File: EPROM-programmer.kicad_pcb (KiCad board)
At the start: 2 copper layers, 139.7 x 139.7 mm, 100 parts, among them J1 ZIF-socket, J10 VCC, J2 ISP, J5 GND, J6 Barrel_Jack_Switch, J7 ZIF_VCC, J8 VPP, J9 GND, P1 USB-C, Q1 BC327, Q2 BC327, Q3 BC327, Q4 BC327, Q5 BC327, Q6 BC327, SW1 Reset, U1 ATmega1284-P, U2 MCP2221AxP, U3 MCP4812, U4 LM358, U5 ULN2003, U6 LM317_TO-220, U7 LM317_TO-220, U8 LM7805_TO220, U9 MC34063AP, Y1 20M

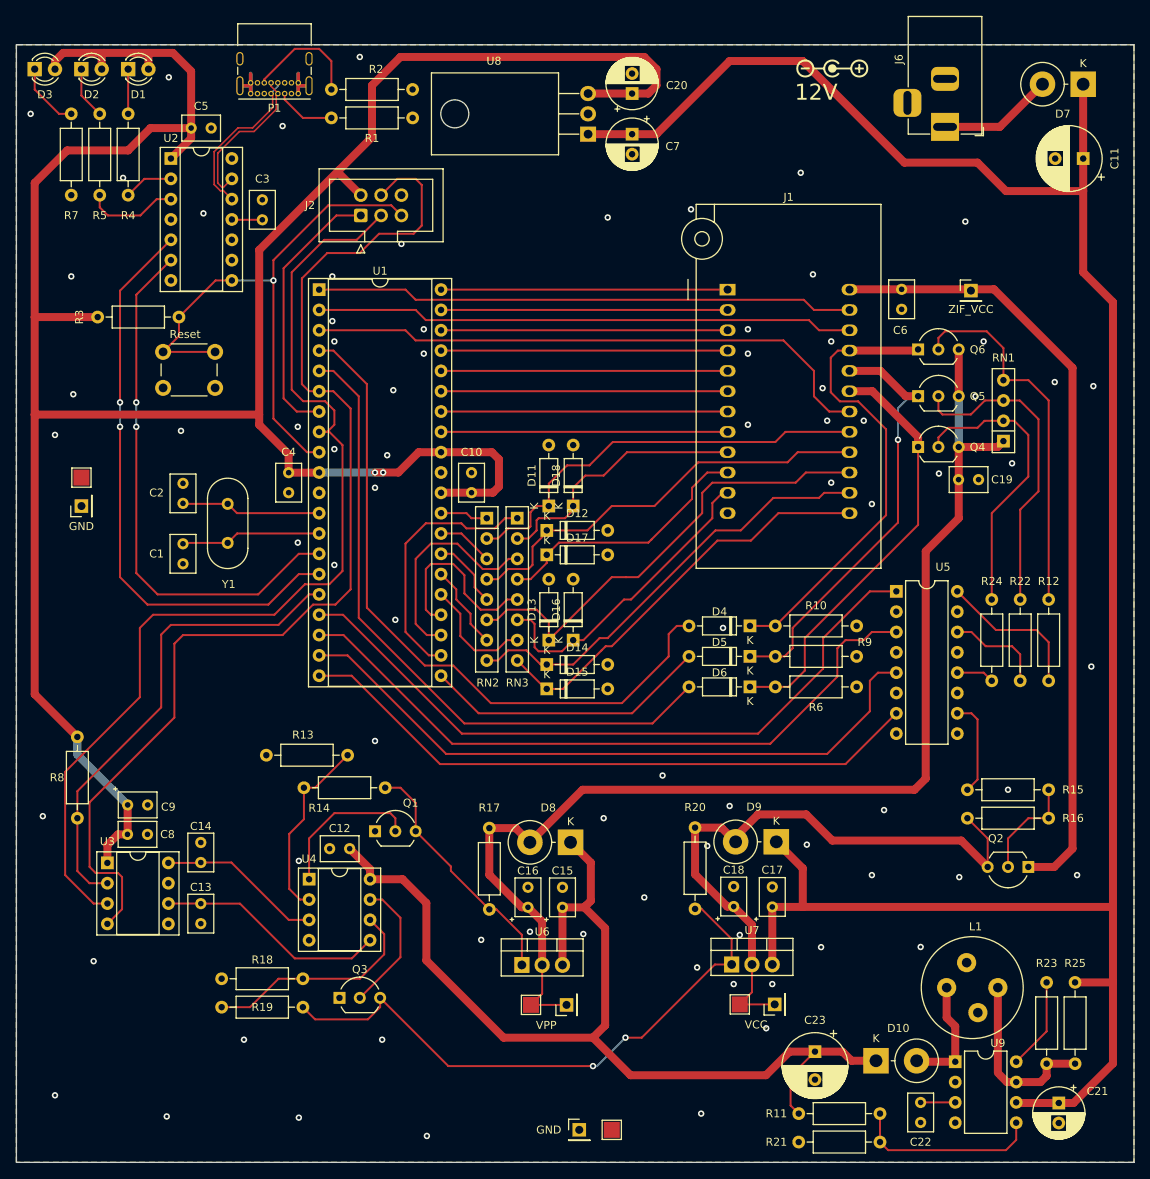
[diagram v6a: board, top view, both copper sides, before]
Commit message: Finish input/output protection on data lines
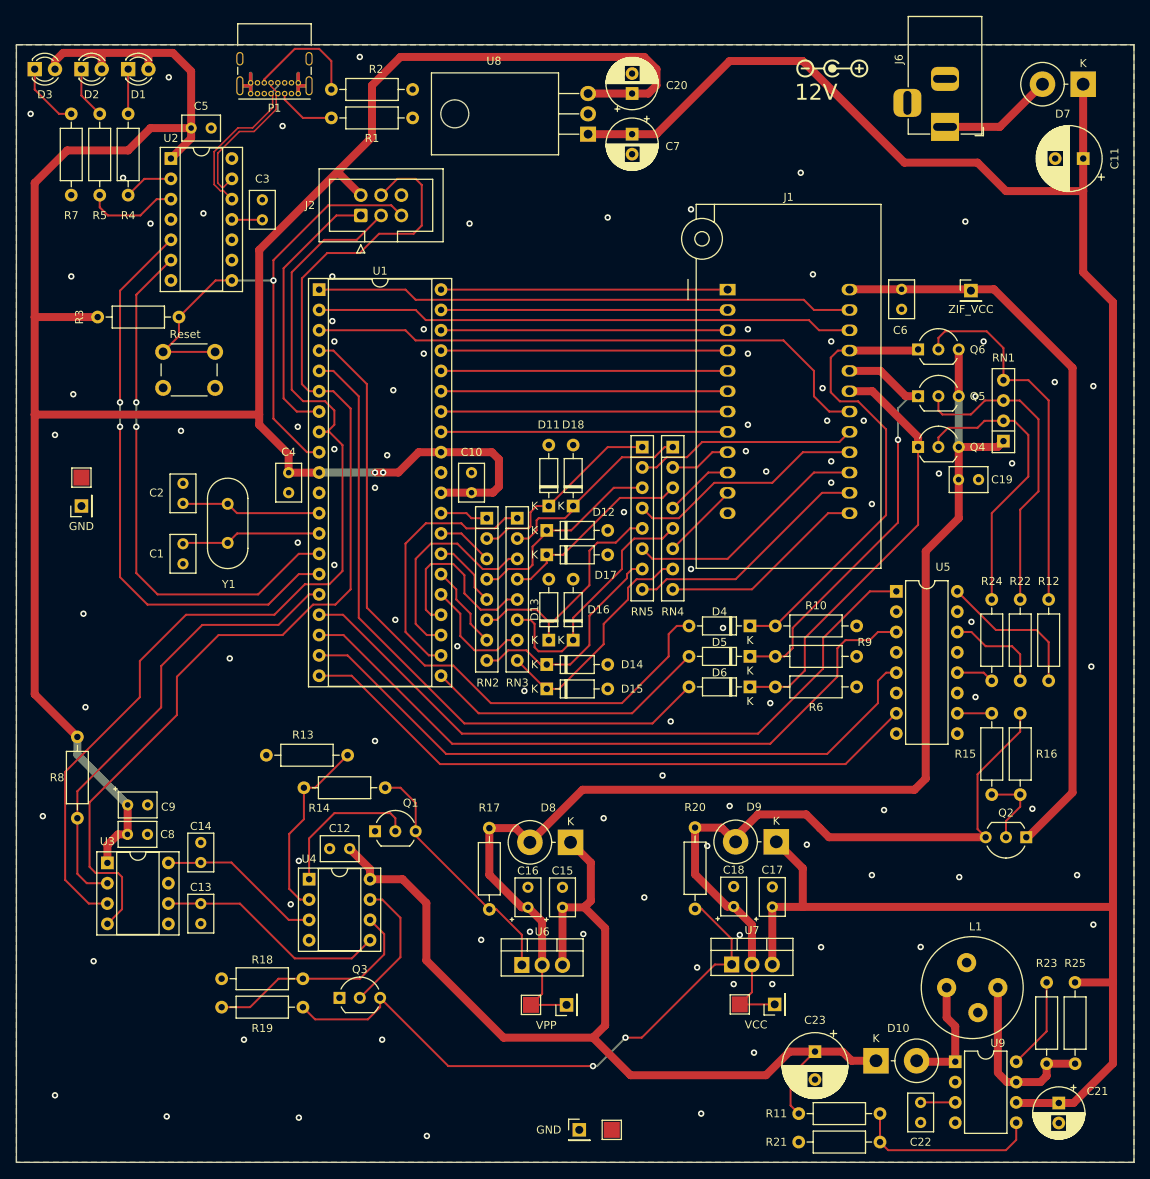
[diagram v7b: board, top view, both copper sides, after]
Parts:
- added RN4: 120, Resistor_THT:R_Array_SIP8, F.Cu at (101.1, 88.4)
- added RN5: 120, Resistor_THT:R_Array_SIP8, F.Cu at (97.3, 88.4)
- moved R16 14.7 mm to (144.5, 121.7), turned to -90 degrees
- moved R15 7.14 mm to (141.0, 131.8), turned to 90 degrees
- moved Q2 3.72 mm to (145.3, 137.2)
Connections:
- D11 pad 1: /Programmer/ZIF_P17 -> Net-(D11-K)
- D12 pad 1: /Programmer/ZIF_P16 -> Net-(D12-K)
- D13 pad 1: /Programmer/ZIF_P15 -> Net-(D13-K)
- D14 pad 1: /Programmer/ZIF_P14 -> Net-(D14-K)
- D15 pad 1: /Programmer/ZIF_P13 -> Net-(D15-K)
- D16 pad 1: /Programmer/ZIF_P11 -> Net-(D16-K)
- D17 pad 1: /Programmer/ZIF_P10 -> Net-(D17-K)
- D18 pad 1: /Programmer/ZIF_P9 -> Net-(D18-K)
- RN2 pad 2: /Programmer/ZIF_P17 -> Net-(D11-K)
- RN2 pad 4: /Programmer/ZIF_P16 -> Net-(D12-K)
- RN2 pad 6: /Programmer/ZIF_P15 -> Net-(D13-K)
- RN2 pad 8: /Programmer/ZIF_P14 -> Net-(D14-K)
- RN3 pad 2: /Programmer/ZIF_P9 -> Net-(D18-K)
- RN3 pad 4: /Programmer/ZIF_P10 -> Net-(D17-K)
- RN3 pad 6: /Programmer/ZIF_P11 -> Net-(D16-K)
- RN3 pad 8: /Programmer/ZIF_P13 -> Net-(D15-K)
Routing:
- net Net-(D16-K): track 0.00 -> 32.1 mm
- net Net-(D13-K): track 0.00 -> 30.8 mm
- net Net-(D15-K): track 0.00 -> 29.5 mm
- net /Programmer/ZIF_P11: track 39.0 -> 9.83 mm
- net Net-(D14-K): track 0.00 -> 28.6 mm
- net /Programmer/ZIF_P15: track 59.5 -> 30.9 mm
- net /Programmer/ZIF_P13: track 53.0 -> 26.0 mm
- net /Programmer/ZIF_P17: track 54.1 -> 27.7 mm
- net Net-(D12-K): track 0.00 -> 26.2 mm
- net Net-(D11-K): track 0.00 -> 25.7 mm
- net /Programmer/ZIF_P9: track 33.1 -> 7.65 mm
- net Net-(D18-K): track 0.00 -> 25.2 mm
- net /Programmer/ZIF_P14: track 56.0 -> 30.9 mm
- net Net-(D17-K): track 0.00 -> 24.8 mm
- net /Programmer/ZIF_P10: track 33.2 -> 8.70 mm
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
